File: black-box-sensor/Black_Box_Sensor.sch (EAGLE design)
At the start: 13 parts, among them U1 ADXL375, U2 ADXL375, U3 ATMEGA32U4-AU, U4 FXAS21002CQR1, U5 MIC5504-3.3YM5-TR, U6 NL27WZ32USG

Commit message: edit schematic
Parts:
- added C5: 0.1uF, rcl:C-USC0603
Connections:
- new net CS1: U1.CS, U6.B1
- new net CS2: U6.B2
- new net MISO: U1.SDO/ALTADDRESS, U4.SA0/MISO
- new net MOSI: U4.SDA/MOSI/SPI_DATA, U6.A1, U6.A2
- new net MOSI1: U1.SDA/SDI/SDIO, U6.Y1
- new net MOSI2: U6.Y2
- new net SCLK: U1.SCL/SCLK, U4.SCL/SCLK
- net 3.3V: now also C5.1, U6.VCC
- net GND: now also C5.2, U6.GND
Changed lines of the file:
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@@
 <setting verticaltext="up"/>
 </settings>
-<grid distance="0.1" unitdist="inch" unit="inch" style="lines" multiple="1" display="yes" altdistance="0.01" altunitdist="inch" altunit="inch"/>
+<grid distance="100" unitdist="mil" unit="mil" style="lines" multiple="1" display="yes" altdistance="10" altunitdist="inch" altunit="inch"/>
 <layers>
 <layer number="1" name="Top" color="4" fill="1" visible="no" active="no"/>
@@
 </part>
 <part name="U6" library="Hocki_Library" deviceset="NL27WZ32USG" device=""/>
+<part name="C5" library="rcl" library_urn="urn:adsk.eagle:library:334" deviceset="C-US" device="C0603" package3d_urn="urn:adsk.eagle:package:23616/2" value="0.1uF">
+<spice>
+<pinmapping spiceprefix="C">
+<pinmap gate="G$1" pin="1" pinorder="1"/>
+<pinmap gate="G$1" pin="2" pinorder="2"/>
+</pinmapping>
+</spice>
+</part>
+<part name="SUPPLY5" library="SparkFun-PowerSymbols" deviceset="3.3V" device=""/>
+<part name="GND3" library="SparkFun-PowerSymbols" deviceset="GND" device=""/>
+<part name="GND7" library="SparkFun-PowerSymbols" deviceset="GND" device=""/>
 </parts>
 <sheets>
@@
 <attribute name="VALUE" x="22.86" y="23.114" size="1.778" layer="96" align="bottom-center"/>
 </instance>
-<instance part="SUPPLY7" gate="G$1" x="12.7" y="0" smashed="yes">
-<attribute name="VALUE" x="12.7" y="2.794" size="1.778" layer="96" align="bottom-center"/>
+<instance part="SUPPLY7" gate="G$1" x="7.62" y="-5.08" smashed="yes">
+<attribute name="VALUE" x="7.62" y="-2.286" size="1.778" layer="96" align="bottom-center"/>
 </instance>
 <instance part="C11" gate="G$1" x="-5.08" y="10.16" smashed="yes">
@@
 <attribute name="NAME" x="-38.1" y="74.93" size="1.778" layer="95" rot="SR0"/>
 <attribute name="VALUE" x="-38.1" y="42.418" size="1.778" layer="96" rot="SR0" align="top-left"/>
+</instance>
+<instance part="C5" gate="G$1" x="-5.08" y="76.2" smashed="yes" rot="R90">
+<attribute name="NAME" x="-5.715" y="79.756" size="1.778" layer="95" rot="R180"/>
+<attribute name="VALUE" x="4.191" y="79.756" size="1.778" layer="96" rot="R180"/>
+</instance>
+<instance part="SUPPLY5" gate="G$1" x="-12.7" y="83.82" smashed="yes">
+<attribute name="VALUE" x="-12.7" y="86.614" size="1.778" layer="96" align="bottom-center"/>
+</instance>
+<instance part="GND3" gate="1" x="2.54" y="71.12" smashed="yes">
+<attribute name="VALUE" x="2.54" y="70.866" size="1.778" layer="96" align="top-center"/>
+</instance>
+<instance part="GND7" gate="1" x="-7.62" y="38.1" smashed="yes">
+<attribute name="VALUE" x="-7.62" y="37.846" size="1.778" layer="96" align="top-center"/>
 </instance>
 </instances>
@@
 <wire x1="68.58" y1="-5.08" x2="63.5" y2="-5.08" width="0.1524" layer="91"/>
 <junction x="63.5" y="-5.08"/>
+</segment>
+<segment>
+<pinref part="C5" gate="G$1" pin="2"/>
+<wire x1="0" y1="76.2" x2="2.54" y2="76.2" width="0.1524" layer="91"/>
+<wire x1="2.54" y1="76.2" x2="2.54" y2="73.66" width="0.1524" layer="91"/>
+<pinref part="GND3" gate="1" pin="GND"/>
+</segment>
+<segment>
+<pinref part="U6" gate="A" pin="GND"/>
+<wire x1="-12.7" y1="45.72" x2="-7.62" y2="45.72" width="0.1524" layer="91"/>
+<wire x1="-7.62" y1="45.72" x2="-7.62" y2="40.64" width="0.1524" layer="91"/>
+<pinref part="GND7" gate="1" pin="GND"/>
 </segment>
 </net>
@@
 <segment>
 <pinref part="U4" gate="G$1" pin="I2C_B/SPI"/>
-<wire x1="22.86" y1="0" x2="12.7" y2="0" width="0.1524" layer="91"/>
-<pinref part="SUPPLY7" gate="G$1" pin="3.3V"/>
 <pinref part="U4" gate="G$1" pin="RST_B"/>
 <wire x1="22.86" y1="-2.54" x2="22.86" y2="0" width="0.1524" layer="91"/>
+<wire x1="22.86" y1="0" x2="17.78" y2="0" width="0.1524" layer="91"/>
 <junction x="22.86" y="0"/>
+<wire x1="17.78" y1="0" x2="17.78" y2="-5.08" width="0.1524" layer="91"/>
+<pinref part="SUPPLY7" gate="G$1" pin="3.3V"/>
+<wire x1="17.78" y1="-5.08" x2="7.62" y2="-5.08" width="0.1524" layer="91"/>
+</segment>
+<segment>
+<pinref part="U6" gate="A" pin="VCC"/>
+<wire x1="-12.7" y1="71.12" x2="-12.7" y2="76.2" width="0.1524" layer="91"/>
+<pinref part="C5" gate="G$1" pin="1"/>
+<wire x1="-12.7" y1="76.2" x2="-12.7" y2="83.82" width="0.1524" layer="91"/>
+<wire x1="-7.62" y1="76.2" x2="-12.7" y2="76.2" width="0.1524" layer="91"/>
+<junction x="-12.7" y="76.2"/>
+<pinref part="SUPPLY5" gate="G$1" pin="3.3V"/>
 </segment>
 </net>
@@
 </segment>
 </net>
+<net name="CS1" class="0">
+<segment>
+<pinref part="U1" gate="ADXL375BCCZ-RL7" pin="CS"/>
+<wire x1="25.4" y1="81.28" x2="20.32" y2="81.28" width="0.1524" layer="91"/>
+<label x="20.32" y="81.28" size="1.27" layer="95" rot="R180" xref="yes"/>
+</segment>
+<segment>
+<pinref part="U6" gate="A" pin="B1"/>
+<wire x1="-43.18" y1="63.5" x2="-48.26" y2="63.5" width="0.1524" layer="91"/>
+<label x="-48.26" y="63.5" size="1.27" layer="95" rot="R180" xref="yes"/>
+</segment>
+</net>
+<net name="SCLK" class="0">
+<segment>
+<pinref part="U1" gate="ADXL375BCCZ-RL7" pin="SCL/SCLK"/>
+<wire x1="25.4" y1="76.2" x2="20.32" y2="76.2" width="0.1524" layer="91"/>
+<label x="20.32" y="76.2" size="1.27" layer="95" rot="R180" xref="yes"/>
+</segment>
+<segment>
+<pinref part="U4" gate="G$1" pin="SCL/SCLK"/>
+<wire x1="22.86" y1="2.54" x2="17.78" y2="2.54" width="0.1524" layer="91"/>
+<label x="17.78" y="2.54" size="1.27" layer="95" rot="R180" xref="yes"/>
+</segment>
+</net>
+<net name="MOSI1" class="0">
+<segment>
+<pinref part="U1" gate="ADXL375BCCZ-RL7" pin="SDA/SDI/SDIO"/>
+<wire x1="25.4" y1="71.12" x2="20.32" y2="71.12" width="0.1524" layer="91"/>
+<label x="20.32" y="71.12" size="1.27" layer="95" rot="R180" xref="yes"/>
+</segment>
+<segment>
+<pinref part="U6" gate="A" pin="Y1"/>
+<wire x1="-12.7" y1="66.04" x2="-7.62" y2="66.04" width="0.1524" layer="91"/>
+<label x="-7.62" y="66.04" size="1.27" layer="95" xref="yes"/>
+</segment>
+</net>
+<net name="MISO" class="0">
+<segment>
+<pinref part="U1" gate="ADXL375BCCZ-RL7" pin="SDO/ALTADDRESS"/>
+<wire x1="71.12" y1="81.28" x2="76.2" y2="81.28" width="0.1524" layer="91"/>
+<label x="76.2" y="81.28" size="1.27" layer="95" xref="yes"/>
+</segment>
+<segment>
+<pinref part="U4" gate="G$1" pin="SA0/MISO"/>
+<wire x1="63.5" y1="12.7" x2="68.58" y2="12.7" width="0.1524" layer="91"/>
+<label x="68.58" y="12.7" size="1.27" layer="95" xref="yes"/>
+</segment>
+</net>
+<net name="MOSI" class="0">
+<segment>
+<pinref part="U6" gate="A" pin="A1"/>
+<wire x1="-43.18" y1="68.58" x2="-55.88" y2="68.58" width="0.1524" layer="91"/>
+<pinref part="U6" gate="A" pin="A2"/>
+<wire x1="-55.88" y1="68.58" x2="-58.42" y2="68.58" width="0.1524" layer="91"/>
+<wire x1="-43.18" y1="53.34" x2="-55.88" y2="53.34" width="0.1524" layer="91"/>
+<wire x1="-55.88" y1="53.34" x2="-55.88" y2="68.58" width="0.1524" layer="91"/>
+<junction x="-55.88" y="68.58"/>
+<label x="-58.42" y="68.58" size="1.27" layer="95" rot="R180" xref="yes"/>
+</segment>
+<segment>
+<pinref part="U4" gate="G$1" pin="SDA/MOSI/SPI_DATA"/>
+<wire x1="22.86" y1="5.08" x2="17.78" y2="5.08" width="0.1524" layer="91"/>
+<label x="17.78" y="5.08" size="1.27" layer="95" rot="R180" xref="yes"/>
+</segment>
+</net>
+<net name="CS2" class="0">
+<segment>
+<pinref part="U6" gate="A" pin="B2"/>
+<wire x1="-43.18" y1="48.26" x2="-48.26" y2="48.26" width="0.1524" layer="91"/>
+<label x="-48.26" y="48.26" size="1.27" layer="95" rot="R180" xref="yes"/>
+</segment>
+</net>
+<net name="MOSI2" class="0">
+<segment>
+<pinref part="U6" gate="A" pin="Y2"/>
+<wire x1="-12.7" y1="50.8" x2="-7.62" y2="50.8" width="0.1524" layer="91"/>
+<label x="-7.62" y="50.8" size="1.27" layer="95" xref="yes"/>
+</segment>
+</net>

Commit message: add to bbs schematic
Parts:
- added C10, C9: 1µF, rcl:C-USC0603
- added C7, C8: 0.1uF, rcl:C-USC0603
- C3, C4, C6: DKPN (none) -> CGA3E2X7R1E104K080AA
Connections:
- new net CS3: U4.SPI_CS_B
- net 3.3V: now also C10.1, C7.1, C8.1, C9.1, U2.VDDI/O, U3.AVCC, U3.AVCC1, U3.UCAP, U3.VCC, U3.VCC1
- net CS1: now also U3.PB0(SS)
- net CS2: now also U2.CS, U3.PB7(OC0A/OC1C/RTS)
- net GND: now also C10.2, C7.2, C8.2, C9.2, U2.GND, U2.VS, U3.GND, U3.GND1, U3.GND2, U3.GND3, U3.UGND
- net MISO: now also U2.SDO/ALTADDRESS, U3.PB3(PDO/MISO)
- net MOSI: now also U3.PB2(PDI/MOSI)
- net MOSI2: now also U2.SDA/SDI/SDIO
- net SCLK: now also U2.SCL/SCLK, U3.PB1(SCK)

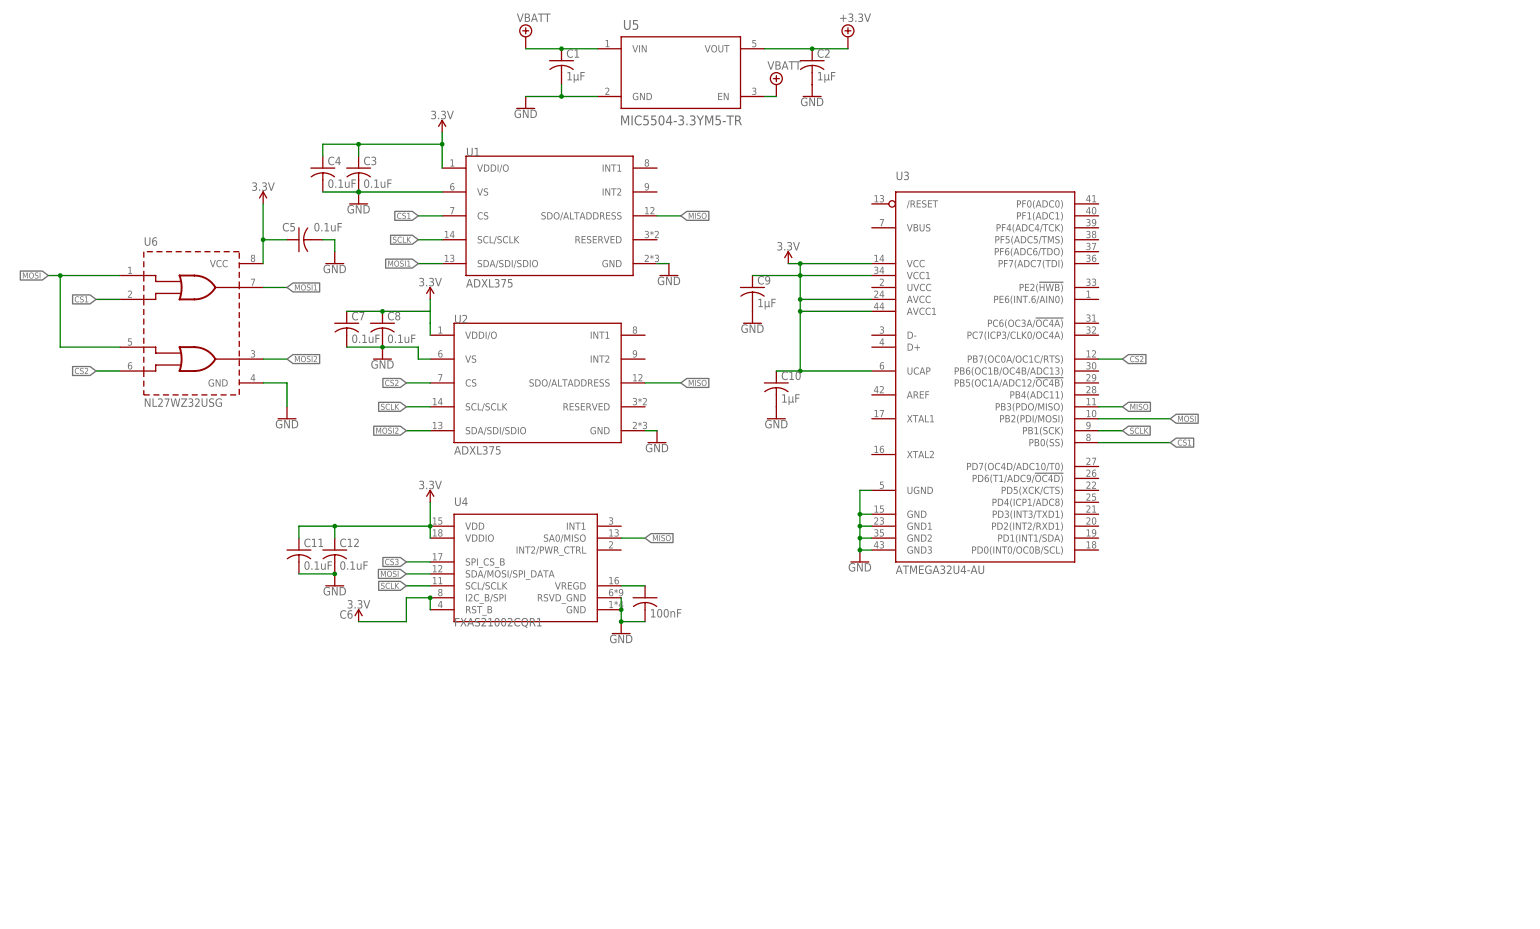
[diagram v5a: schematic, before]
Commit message: add us and sd card reader
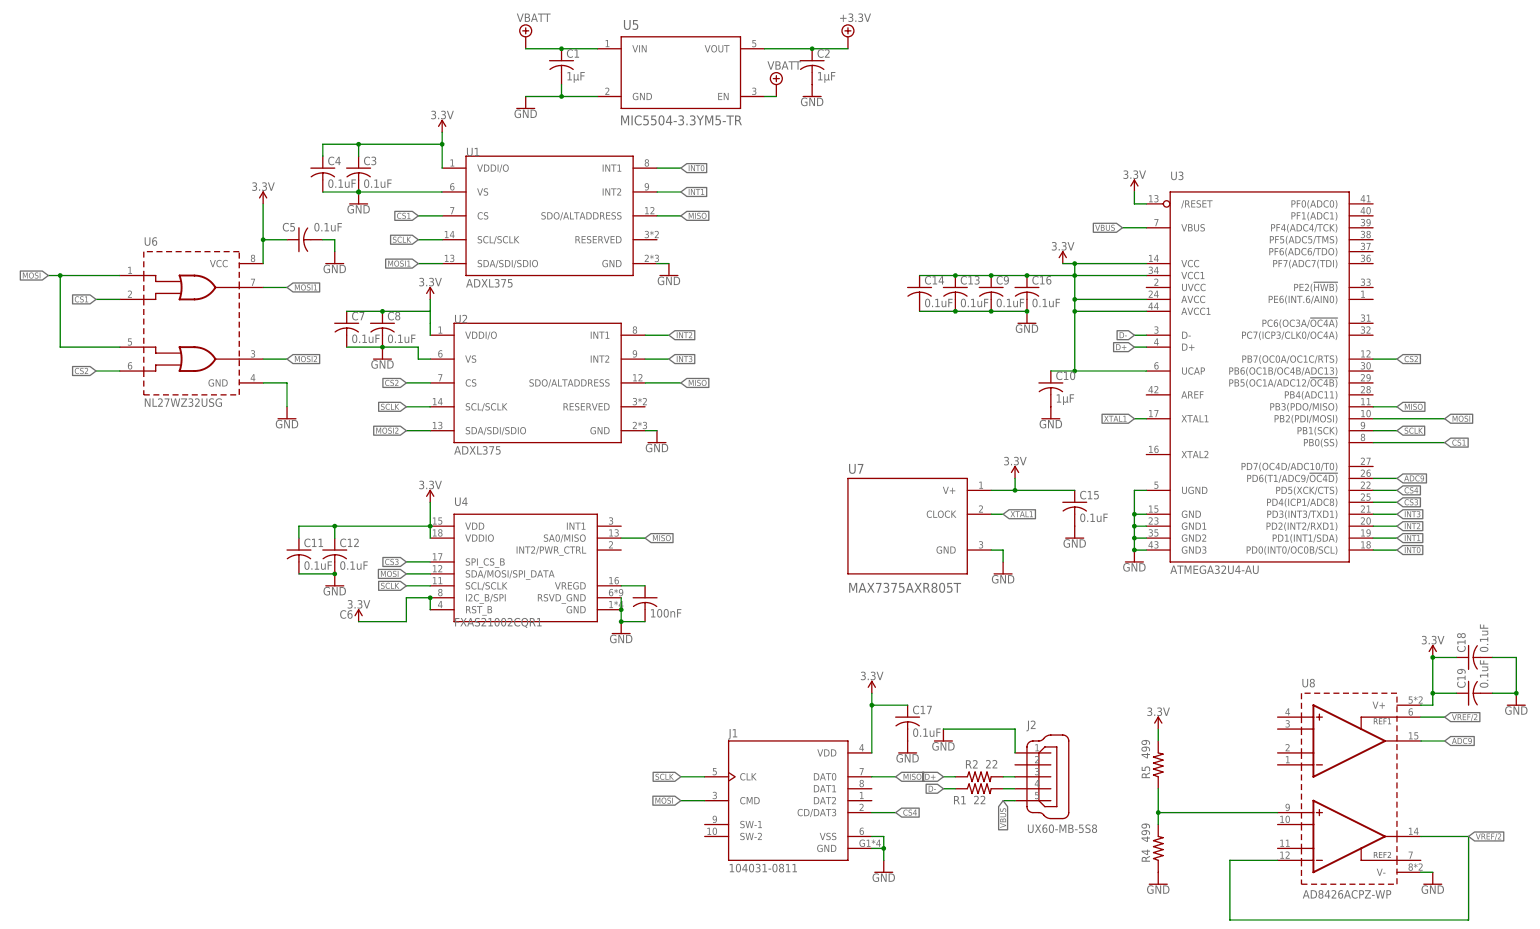
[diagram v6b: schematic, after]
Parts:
- added C13, C14, C15, C16, C17, C18, C19: 0.1uF, rcl:C-USC0603
- added J1: 104031-0811, BBS_Library:104031-0811
- added J2: UX60-MB-5S8, BBS_Library:UX60-MB-5S8
- added R1, R2: 22, rcl:R-US_R0603
- added R4, R5: 499, rcl:R-US_R0603
- added U7: MAX7375AXR805T, BBS_Library:MAX7375AXR805T
- added U8: AD8426ACPZ-WP, BBS_Library:AD8426ACPZ-WP
- C9: value 1µF -> 0.1uF; DKPN CC0603KRX7R6BB105 -> CGA3E2X7R1E104K080AA; VOLTAGE 10V -> (none)
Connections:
- new net ADC9: U3.PD6(T1/ADC9/!OC4D), U8.OUTA
- new net CS4: J1.CD/DAT3, U3.PD5(XCK/CTS)
- new net D+: J2.3, R2.1, R2.2, U3.D+
- new net D-: J2.4, R1.1, R1.2, U3.D-
- new net INT0: U1.INT1, U3.PD0(INT0/OC0B/SCL)
- new net INT1: U1.INT2, U3.PD1(INT1/SDA)
- new net INT2: U2.INT1, U3.PD2(INT2/RXD1)
- new net INT3: U2.INT2, U3.PD3(INT3/TXD1)
- new net N$4: R4.2, R5.1, U8.INB+
- new net VBUS: J2.5, U3.VBUS
- new net VREF/2: U8.INB-, U8.OUTB, U8.REFA
- new net XTAL1: U3.XTAL1, U7.CLOCK
- net 3.3V: now also C13.1, C14.1, C15.1, C16.1, C17.1, C18.1, C19.1, J1.VDD, R5.2, U3./RESET, U7.V+, U8.V+
- net CS3: now also U3.PD4(ICP1/ADC8)
- net GND: now also C13.2, C14.2, C15.2, C16.2, C17.2, C18.2, C19.2, J1.GND, J1.VSS, J2.1, R4.1, U7.GND, U8.V-
- net MISO: now also J1.DAT0
- net MOSI: now also J1.CMD
- net SCLK: now also J1.CLK
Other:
- moved on the sheet: C10, C9, U3

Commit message: finish schematic for bbs
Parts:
- added J3: B4B-PH-SM4-TBT(LF)(SN), BBS_Library:B4B-PH-SM4-TBT(LF)(SN)
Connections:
- new net V+: J3.2, U8.INA+
- new net V-: J3.3, U8.INA-
- net 3.3V: now also J3.1
- net GND: now also J3.4, J3.ANCHOR
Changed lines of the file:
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@@
 <part name="SUPPLY14" library="SparkFun-PowerSymbols" deviceset="3.3V" device=""/>
 <part name="GND21" library="SparkFun-PowerSymbols" deviceset="GND" device=""/>
+<part name="J3" library="BBS_Library" deviceset="B4B-PH-SM4-TBT(LF)(SN)" device=""/>
+<part name="SUPPLY15" library="SparkFun-PowerSymbols" deviceset="3.3V" device=""/>
+<part name="GND22" library="SparkFun-PowerSymbols" deviceset="GND" device=""/>
 </parts>
 <sheets>
@@
 <instance part="GND21" gate="1" x="177.8" y="-60.96" smashed="yes">
 <attribute name="VALUE" x="177.8" y="-61.214" size="1.778" layer="96" align="top-center"/>
+</instance>
+<instance part="J3" gate="A" x="33.02" y="-35.56" smashed="yes">
+<attribute name="NAME" x="37.1856" y="-30.2514" size="2.0828" layer="95" ratio="6" rot="SR0"/>
+<attribute name="VALUE" x="36.83" y="-51.816" size="2.0828" layer="96" ratio="6"/>
+</instance>
+<instance part="SUPPLY15" gate="G$1" x="27.94" y="-30.48" smashed="yes">
+<attribute name="VALUE" x="27.94" y="-27.686" size="1.778" layer="96" align="bottom-center"/>
+</instance>
+<instance part="GND22" gate="1" x="27.94" y="-48.26" smashed="yes">
+<attribute name="VALUE" x="27.94" y="-48.514" size="1.778" layer="96" align="top-center"/>
 </instance>
 </instances>
@@
 <pinref part="R4" gate="G$1" pin="1"/>
 <pinref part="GND21" gate="1" pin="GND"/>
+</segment>
+<segment>
+<pinref part="J3" gate="A" pin="ANCHOR"/>
+<pinref part="GND22" gate="1" pin="GND"/>
+<wire x1="33.02" y1="-45.72" x2="27.94" y2="-45.72" width="0.1524" layer="91"/>
+<pinref part="J3" gate="A" pin="4"/>
+<wire x1="33.02" y1="-43.18" x2="27.94" y2="-43.18" width="0.1524" layer="91"/>
+<wire x1="27.94" y1="-43.18" x2="27.94" y2="-45.72" width="0.1524" layer="91"/>
+<junction x="27.94" y="-45.72"/>
 </segment>
 </net>
@@
 <wire x1="177.8" y1="-27.94" x2="177.8" y2="-30.48" width="0.1524" layer="91"/>
 </segment>
+<segment>
+<pinref part="SUPPLY15" gate="G$1" pin="3.3V"/>
+<wire x1="27.94" y1="-30.48" x2="27.94" y2="-35.56" width="0.1524" layer="91"/>
+<pinref part="J3" gate="A" pin="1"/>
+<wire x1="27.94" y1="-35.56" x2="33.02" y2="-35.56" width="0.1524" layer="91"/>
+</segment>
 </net>
 <net name="N$1" class="0">
@@
 </segment>
 </net>
+<net name="V+" class="0">
+<segment>
+<pinref part="J3" gate="A" pin="2"/>
+<wire x1="33.02" y1="-38.1" x2="27.94" y2="-38.1" width="0.1524" layer="91"/>
+<label x="27.94" y="-38.1" size="1.27" layer="95" rot="R180" xref="yes"/>
+</segment>
+<segment>
+<pinref part="U8" gate="G$1" pin="INA+"/>
+<wire x1="203.2" y1="-25.4" x2="198.12" y2="-25.4" width="0.1524" layer="91"/>
+<label x="198.12" y="-25.4" size="1.27" layer="95" rot="R180" xref="yes"/>
+</segment>
+</net>
+<net name="V-" class="0">
+<segment>
+<pinref part="J3" gate="A" pin="3"/>
+<wire x1="33.02" y1="-40.64" x2="27.94" y2="-40.64" width="0.1524" layer="91"/>
+<label x="27.94" y="-40.64" size="1.27" layer="95" rot="R180" xref="yes"/>
+</segment>
+<segment>
+<pinref part="U8" gate="G$1" pin="INA-"/>
+<wire x1="203.2" y1="-35.56" x2="198.12" y2="-35.56" width="0.1524" layer="91"/>
+<label x="198.12" y="-35.56" size="1.27" layer="95" rot="R180" xref="yes"/>
+</segment>
+</net>

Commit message: update black box sensor
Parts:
- added CN1: (no value), Hocki_Library:JST_2PIN
- added LED1: (no value), led:LEDCHIP-LED0805
- added LED2: (no value), led:LEDKA-3528ASYC
- added R3, R6: 100, rcl:R-US_R0603
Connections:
- removed net +3.3V: C2.1, U5.VOUT
- removed net ADC9: U3.PD6(T1/ADC9/!OC4D), U8.OUTA
- new net CURRENT: U3.PD7(OC4D/ADC10/T0), U8.OUTA
- new net LED: LED2.A, U3.PD6(T1/ADC9/!OC4D)
- new net N$2: J2.3, R2.2
- new net N$3: J2.4, R1.2
- new net N$5: LED2.C, R3.2
- new net N$6: LED1.C, R6.1
- net 3.3V: now also C2.1, LED1.A, U5.VOUT
- net D+: no longer J2.3, R2.2
- net D-: no longer J2.4, R1.2
- net GND: now also CN1.2, CN1.SHIELD, R3.1, R6.2
- net VBATT: now also CN1.1
